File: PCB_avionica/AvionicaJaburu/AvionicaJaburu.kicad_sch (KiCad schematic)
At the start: 29 parts, among them J1 Screw_Terminal_01x02, J2 Screw_Terminal_01x02, J3 RESET, J4 Conn_01x08_Pin, J5 VDD, Q1 NMOS_Substrate, Q2 NMOS_Substrate, U1 AMS1117-3.3, U2 ESP32-DEVKIT-V1

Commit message: Aviônica Jaburu pino buzzer atualizado
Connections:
- net BZR: now also U2.22 (D33); no longer U2.20 (D35)
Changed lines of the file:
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@@
+		)
+	)
+	(global_label "BZR"
+		(shape input)
+		(at 179.07 62.23 0)
+		(fields_autoplaced yes)
+		(effects
+			(font
+				(size 1.27 1.27)
+			)
+			(justify left)
+		)
+		(property "Intersheetrefs" "${INTERSHEET_REFS}"
+			(at 185.8047 62.23 0)
+			(effects
+				(font
+					(size 1.27 1.27)
+				)
+				(justify left)
+				(hide yes)
+			)
 		)
 	)
@@
 			(effects
 				(font
-					(size 1.27 1.27)
-				)
-				(justify left)
-				(hide yes)
-			)
-		)
-	)
-	(global_label "BZR"
-		(shape input)
-		(at 179.07 64.77 0)
-		(fields_autoplaced yes)
-		(effects
-			(font
-				(size 1.27 1.27)
-			)
-			(justify left)
-		)
-		(property "Intersheetrefs" "${INTERSHEET_REFS}"
-			(at 185.8047 64.77 0)
-			(effects
-				(font

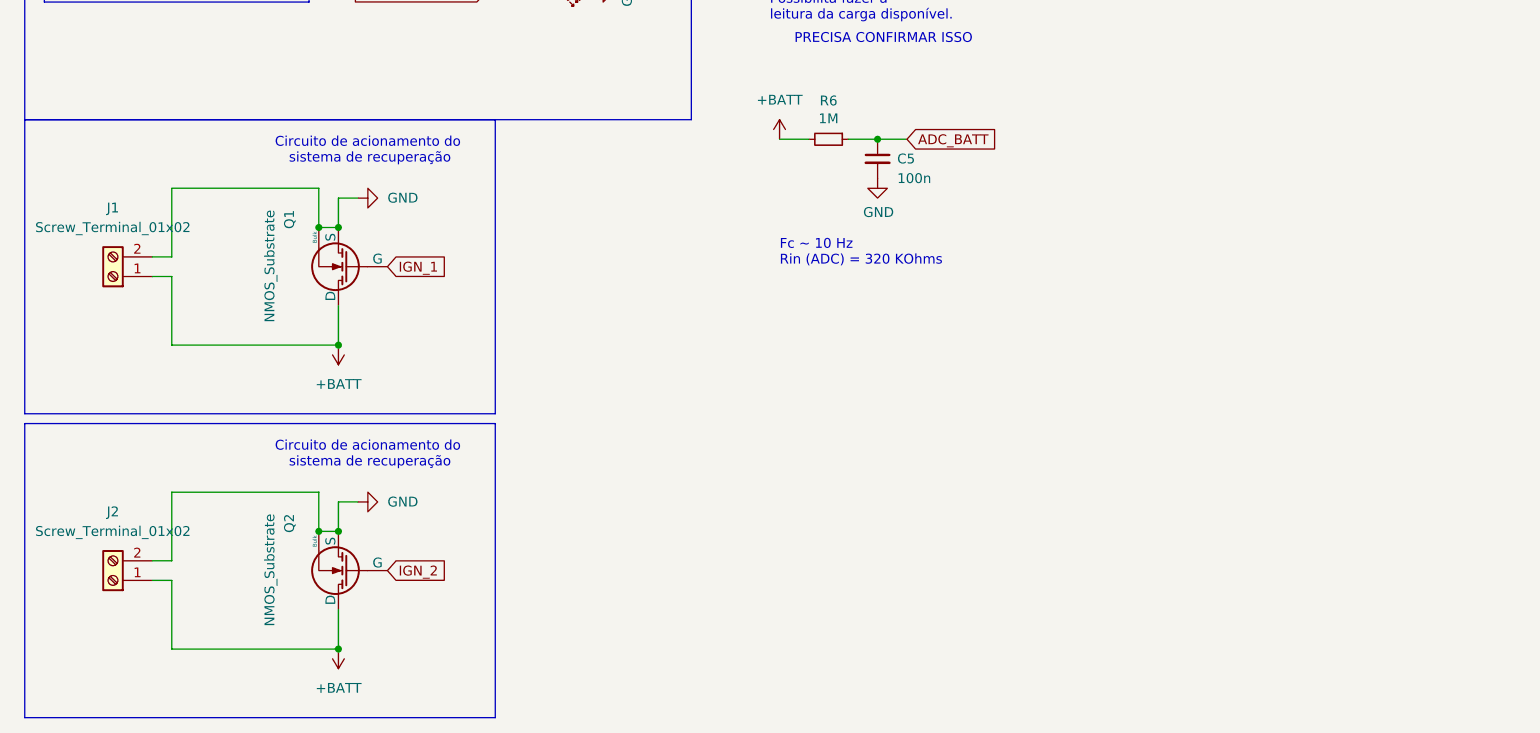
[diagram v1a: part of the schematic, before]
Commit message: Aviônica com furações e MOSFET atualizados
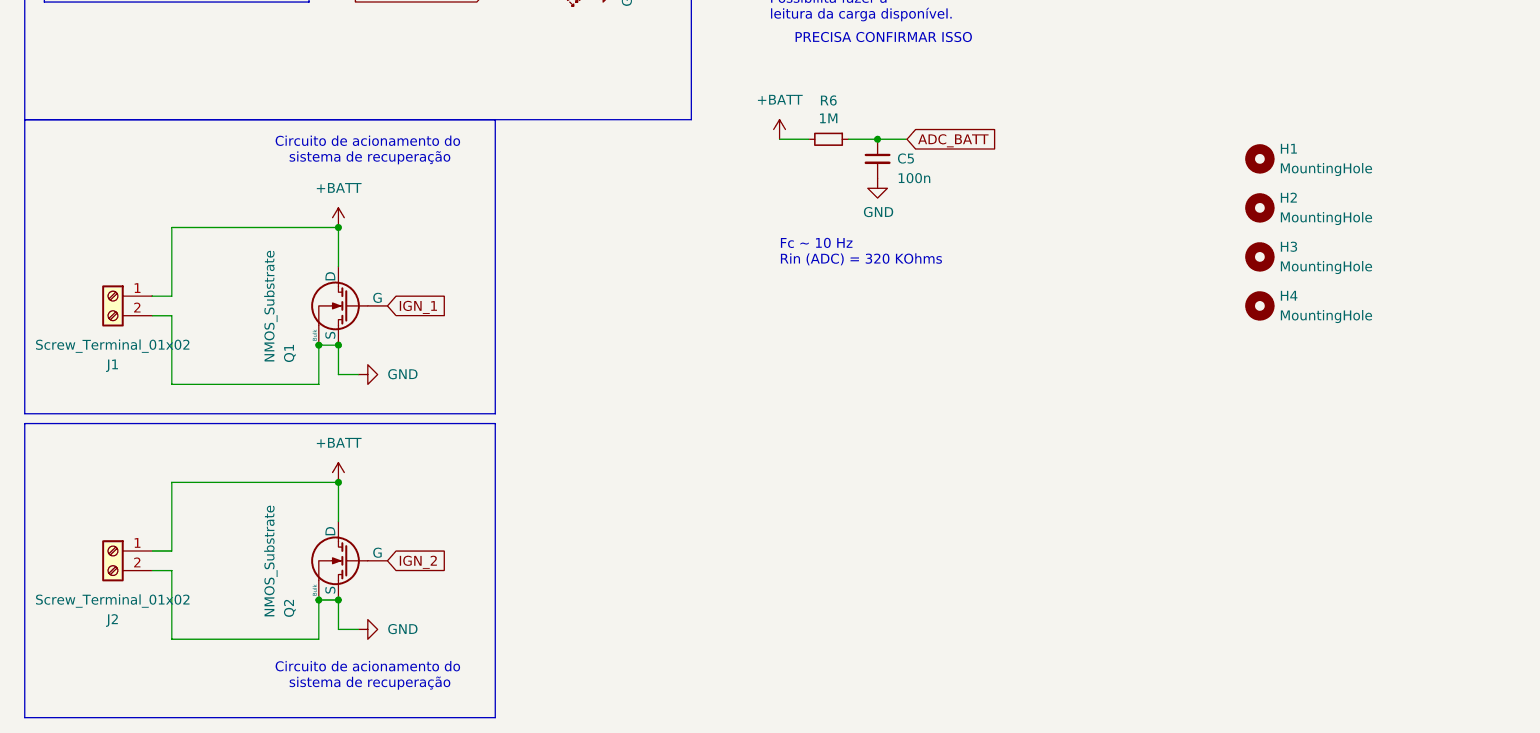
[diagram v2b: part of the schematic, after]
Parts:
- added H1, H2, H3, H4: MountingHole, MountingHole:MountingHole_3.2mm_M3, symbol Mechanical:MountingHole
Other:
- moved on the sheet: J1, J2, Q1, Q2
